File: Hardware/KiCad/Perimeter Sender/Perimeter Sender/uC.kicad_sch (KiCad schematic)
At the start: 15 parts, among them J3 Conn_02x05_Row_Letter_Last, U1 AVR128DA48x-xPT, U3 WeMos_D1_mini, Y1 32.768kHz

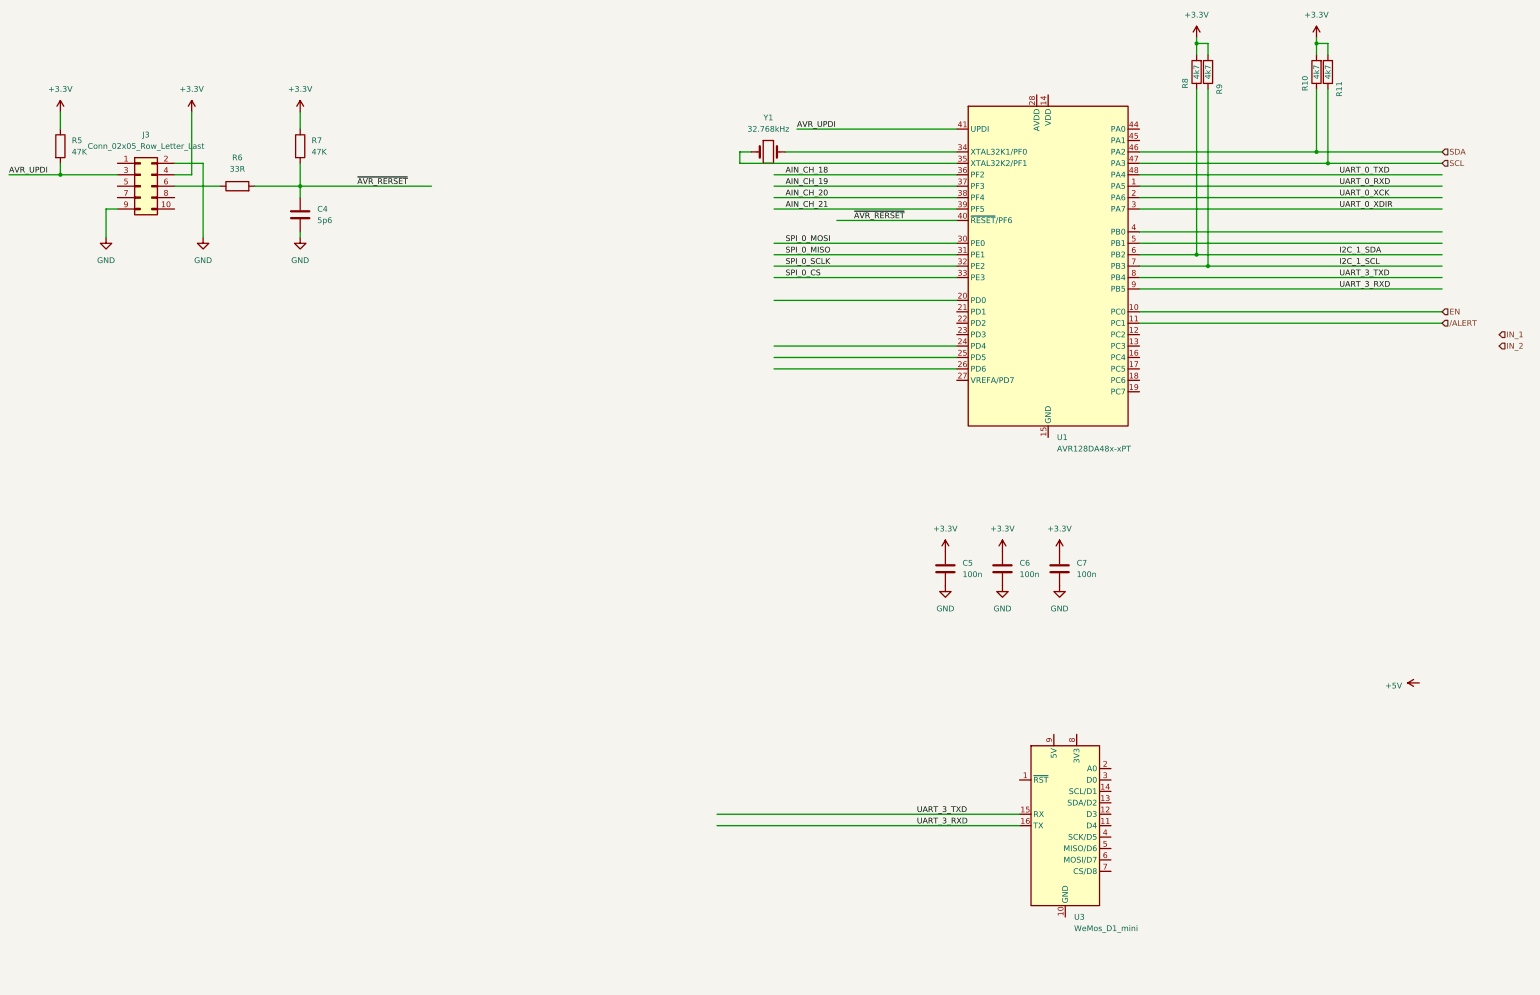
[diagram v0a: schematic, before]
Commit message: Redesign: - Controller - I2C pinning geändert - uvm
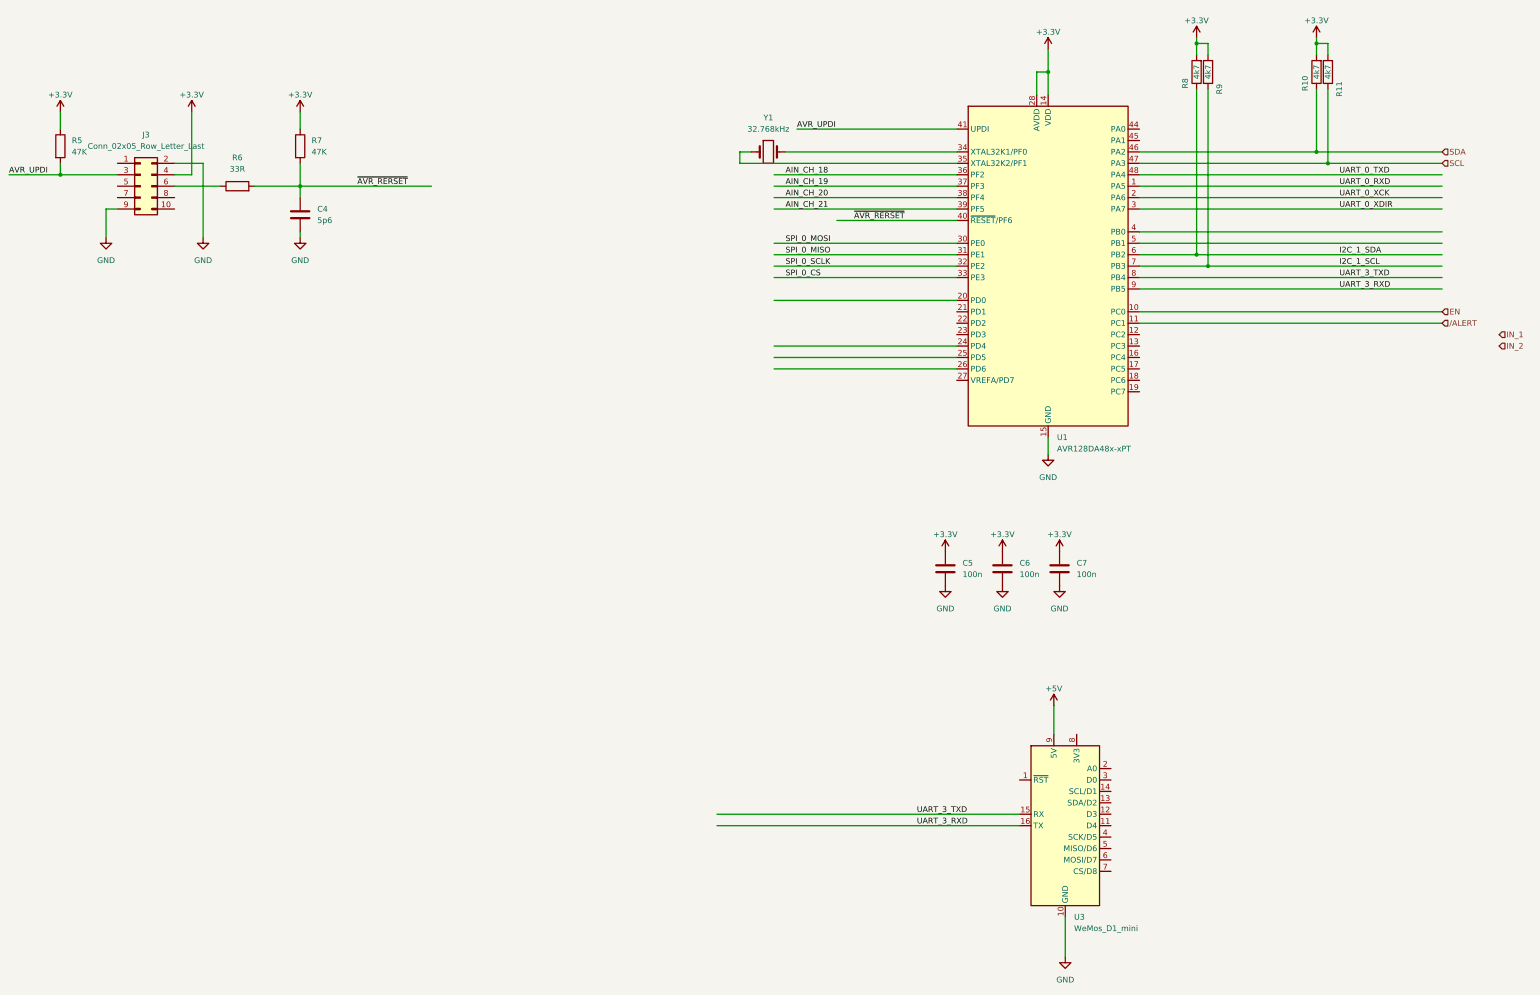
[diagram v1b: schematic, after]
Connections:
- net +3.3V: now also U1.14 (VDD), U1.28 (AVDD), U1.42 (VDD)
- net +5V: now also U3.9 (5V)
- net GND: now also U1.15 (GND), U1.29 (GND), U1.43 (GND), U3.10 (GND)
